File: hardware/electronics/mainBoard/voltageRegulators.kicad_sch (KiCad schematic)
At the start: 44 parts, among them J28 Conn_01x04_Pin, J29 Conn_01x04_Pin, Q10 BSS138-7-F, Q11 BSS138-7-F, Q8 CSD17581Q3A, Q9 CSD17581Q3A, U23 LM25148-Q1, U24 TPS62A01

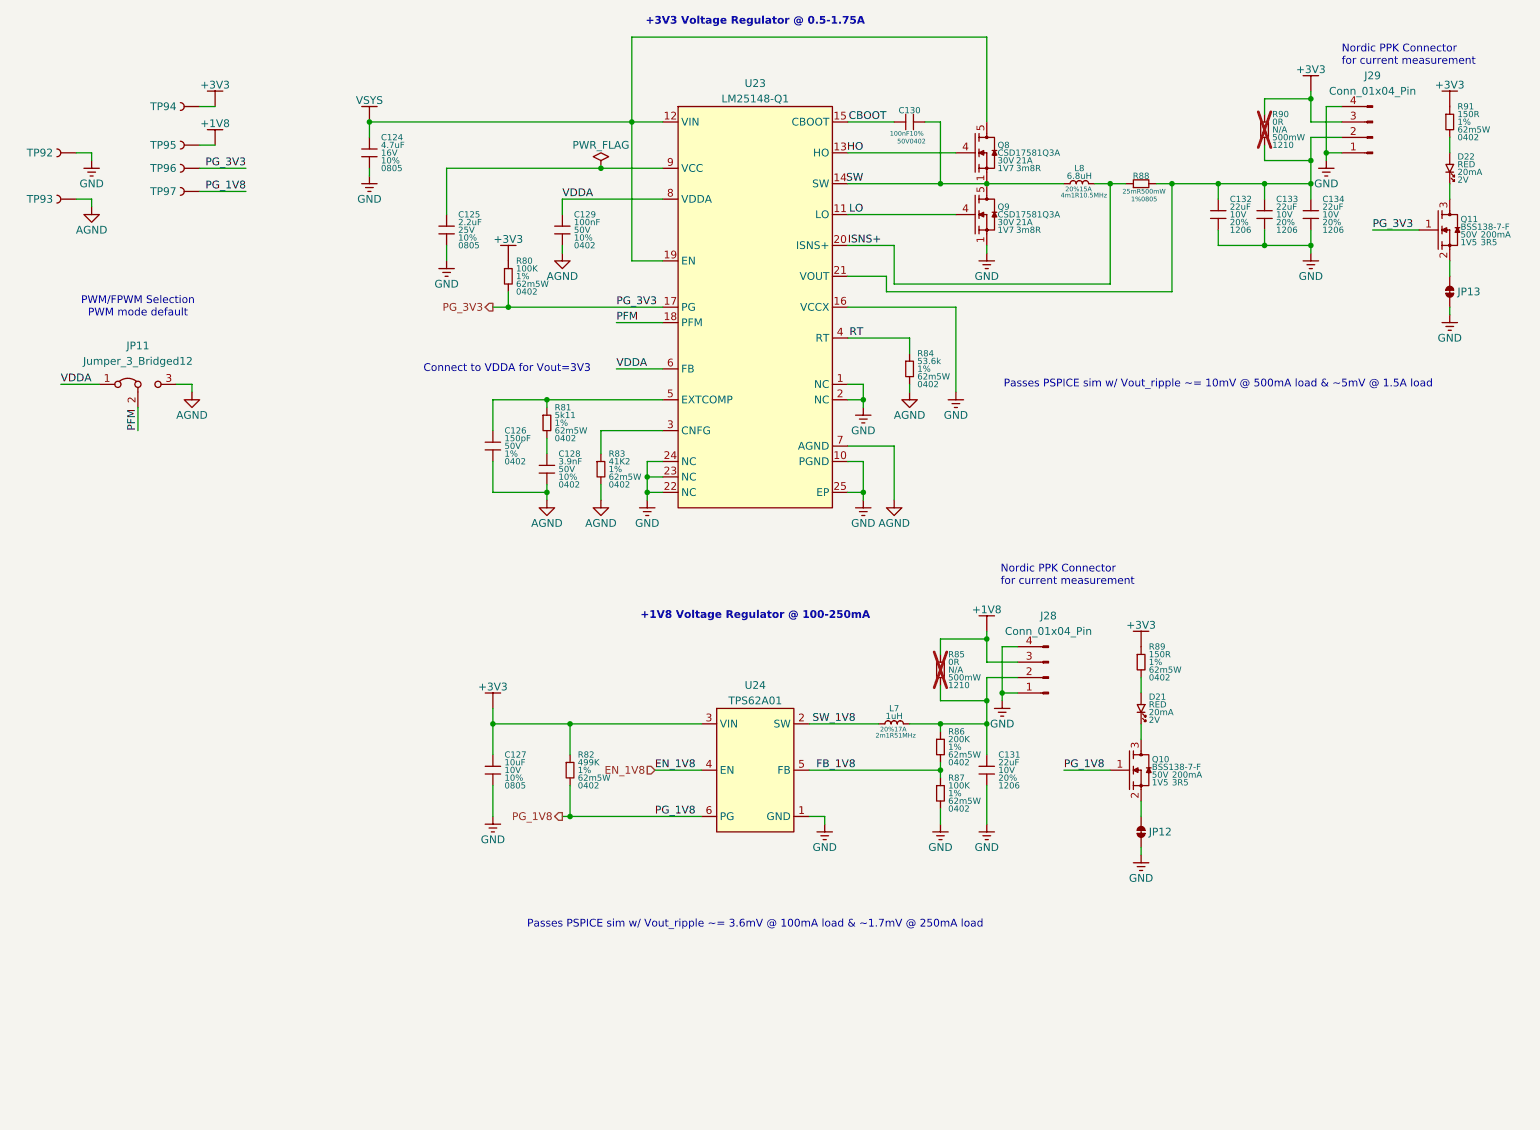
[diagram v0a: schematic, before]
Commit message: updated symbol refs
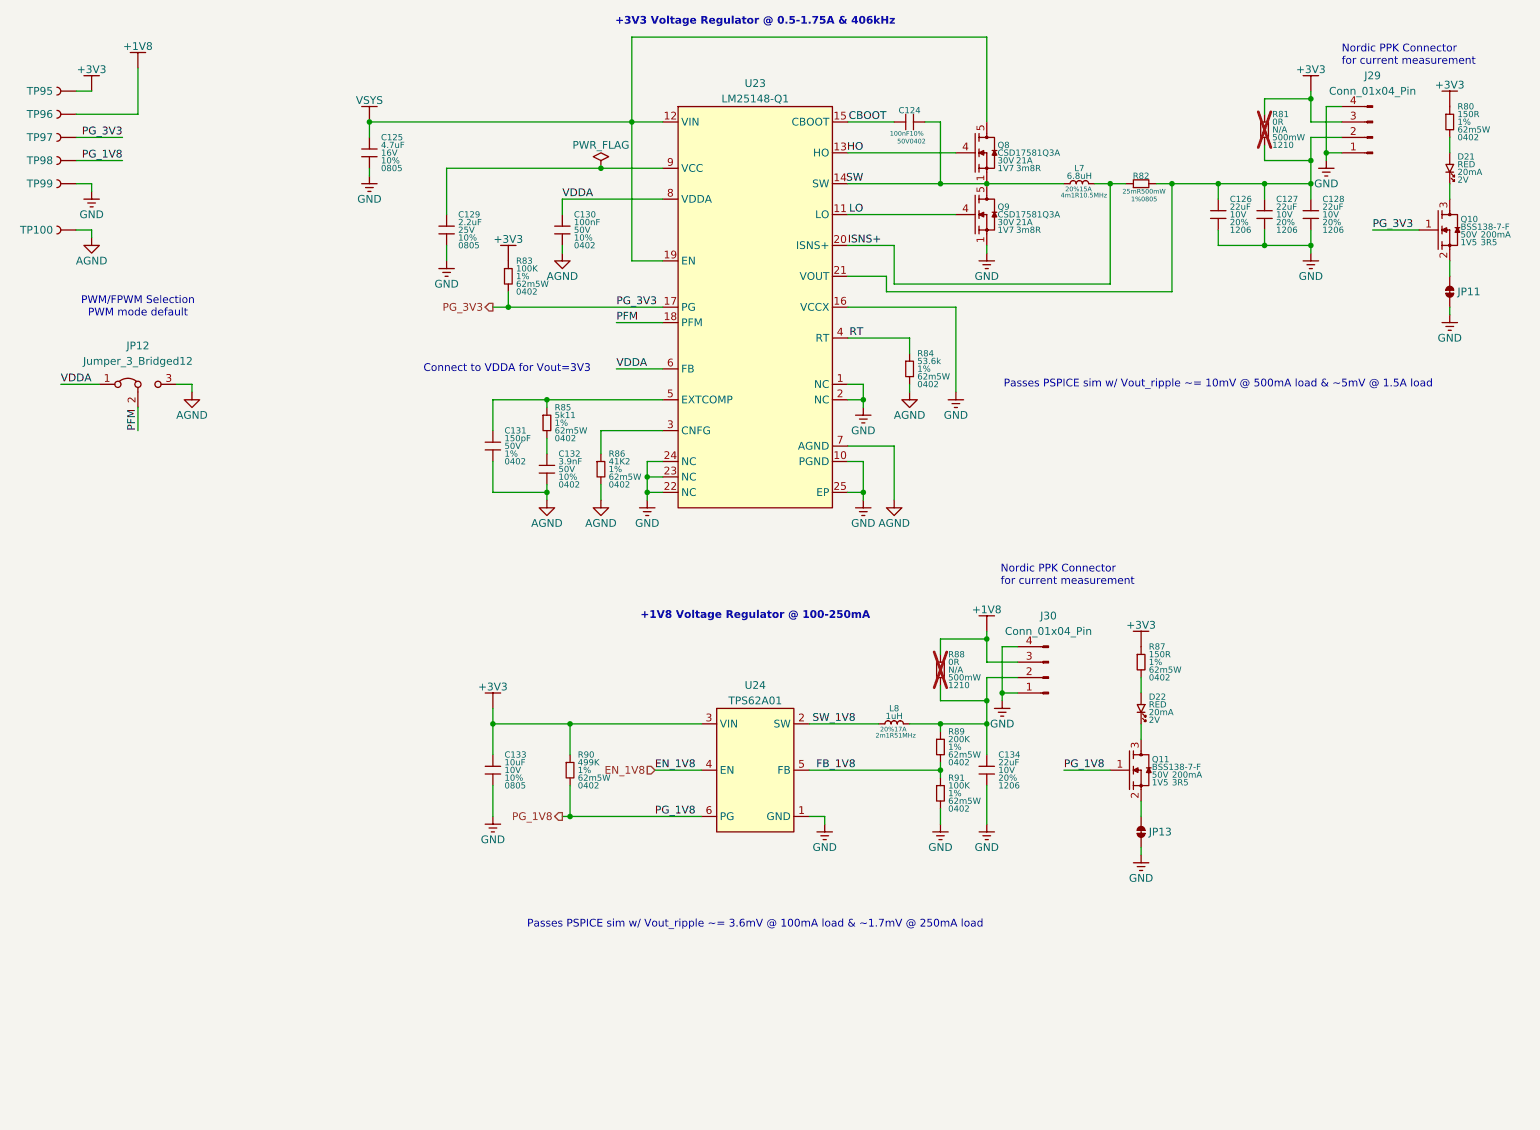
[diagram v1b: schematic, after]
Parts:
- renumbered C130 to C124, C124 to C125, C132 to C126, C133 to C127, C134 to C128, C125 to C129, C129 to C130, C126 to C131, C128 to C132, C127 to C133, C131 to C134, D22 to D21, D21 to D22, J28 to J30, JP13 to JP11, JP11 to JP12, JP12 to JP13, L8 to L7, L7 to L8, Q11 to Q10, Q10 to Q11, R91 to R80, R90 to R81, R88 to R82, R80 to R83, R81 to R85, R83 to R86, R89 to R87, R85 to R88, R86 to R89, R82 to R90, R87 to R91, TP93 to TP100, TP94 to TP95, TP95 to TP96, TP96 to TP97, TP97 to TP98, TP92 to TP99
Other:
- note added: "+3V3 Voltage Regulator @ 0.5-1.75A & 406kHz"
- note removed: "+3V3 Voltage Regulator @ 0.5-1.75A"
- moved on the sheet: TP100, TP95, TP96, TP97, TP98, TP99

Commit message: assigned FPs
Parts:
- L7: footprint (none) -> lib_passives:WE-XHMI-1510
- Q8, Q9: footprint (none) -> lib_ICs:SON65P300X315X90-8
- U23: footprint (none) -> lib_ICs:QFN50P350X550X100-24
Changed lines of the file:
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@@
 			)
 		)
-		(property "Footprint" ""
+		(property "Footprint" "lib_ICs:QFN50P350X550X100-24"
 			(at 139.7 63.5 0)
 			(effects
@@
 			)
 		)
-		(property "Footprint" ""
+		(property "Footprint" "lib_ICs:SON65P300X315X90-8"
 			(at 180.34 40.005 90)
 			(effects
@@
 			)
 		)
-		(property "Footprint" ""
+		(property "Footprint" "lib_passives:WE-XHMI-1510"
 			(at 191.77 43.18 0)
 			(effects
@@
 			)
 		)
-		(property "Footprint" ""
+		(property "Footprint" "lib_ICs:SON65P300X315X90-8"
 			(at 180.34 50.165 90)
 			(effects

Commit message: added footprints to symbols
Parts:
- J29, J30: footprint (none) -> lib_connectors:conn_01x04_254_right_angle
- JP12: footprint (none) -> lib_passives:SolderJumper-3_P1.3mm_Bridged12_RoundedPad1.0x1.5mm
- L8: footprint (none) -> lib_passives:WE-XHMI-8080
- Q10, Q11: footprint (none) -> lib_ICs:SOT23
- U24: footprint (none) -> lib_ICs:SOT563
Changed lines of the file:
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@@
 			)
 		)
-		(property "Footprint" ""
+		(property "Footprint" "lib_passives:WE-XHMI-8080"
 			(at 161.29 132.08 0)
 			(effects
@@
 			)
 		)
-		(property "Footprint" ""
+		(property "Footprint" "lib_ICs:SOT23"
 			(at 205.74 141.605 90)
 			(effects
@@
 			)
 		)
-		(property "Footprint" ""
+		(property "Footprint" "lib_connectors:conn_01x04_254_right_angle"
 			(at 241.3 35.56 0)
 			(effects
@@
 			)
 		)
-		(property "Footprint" ""
+		(property "Footprint" "lib_connectors:conn_01x04_254_right_angle"
 			(at 187.96 124.46 0)
 			(effects
@@
 			)
 		)
-		(property "Footprint" ""
+		(property "Footprint" "lib_passives:SolderJumper-3_P1.3mm_Bridged12_RoundedPad1.0x1.5mm"
 			(at 38.1 76.2 0)
 			(effects
@@
 			)
 		)
-		(property "Footprint" ""
+		(property "Footprint" "lib_ICs:SOT563"
 			(at 139.7 139.7 0)
 			(effects
@@
 			)
 		)
-		(property "Footprint" ""
+		(property "Footprint" "lib_ICs:SOT23"
 			(at 256.54 52.705 90)
 			(effects

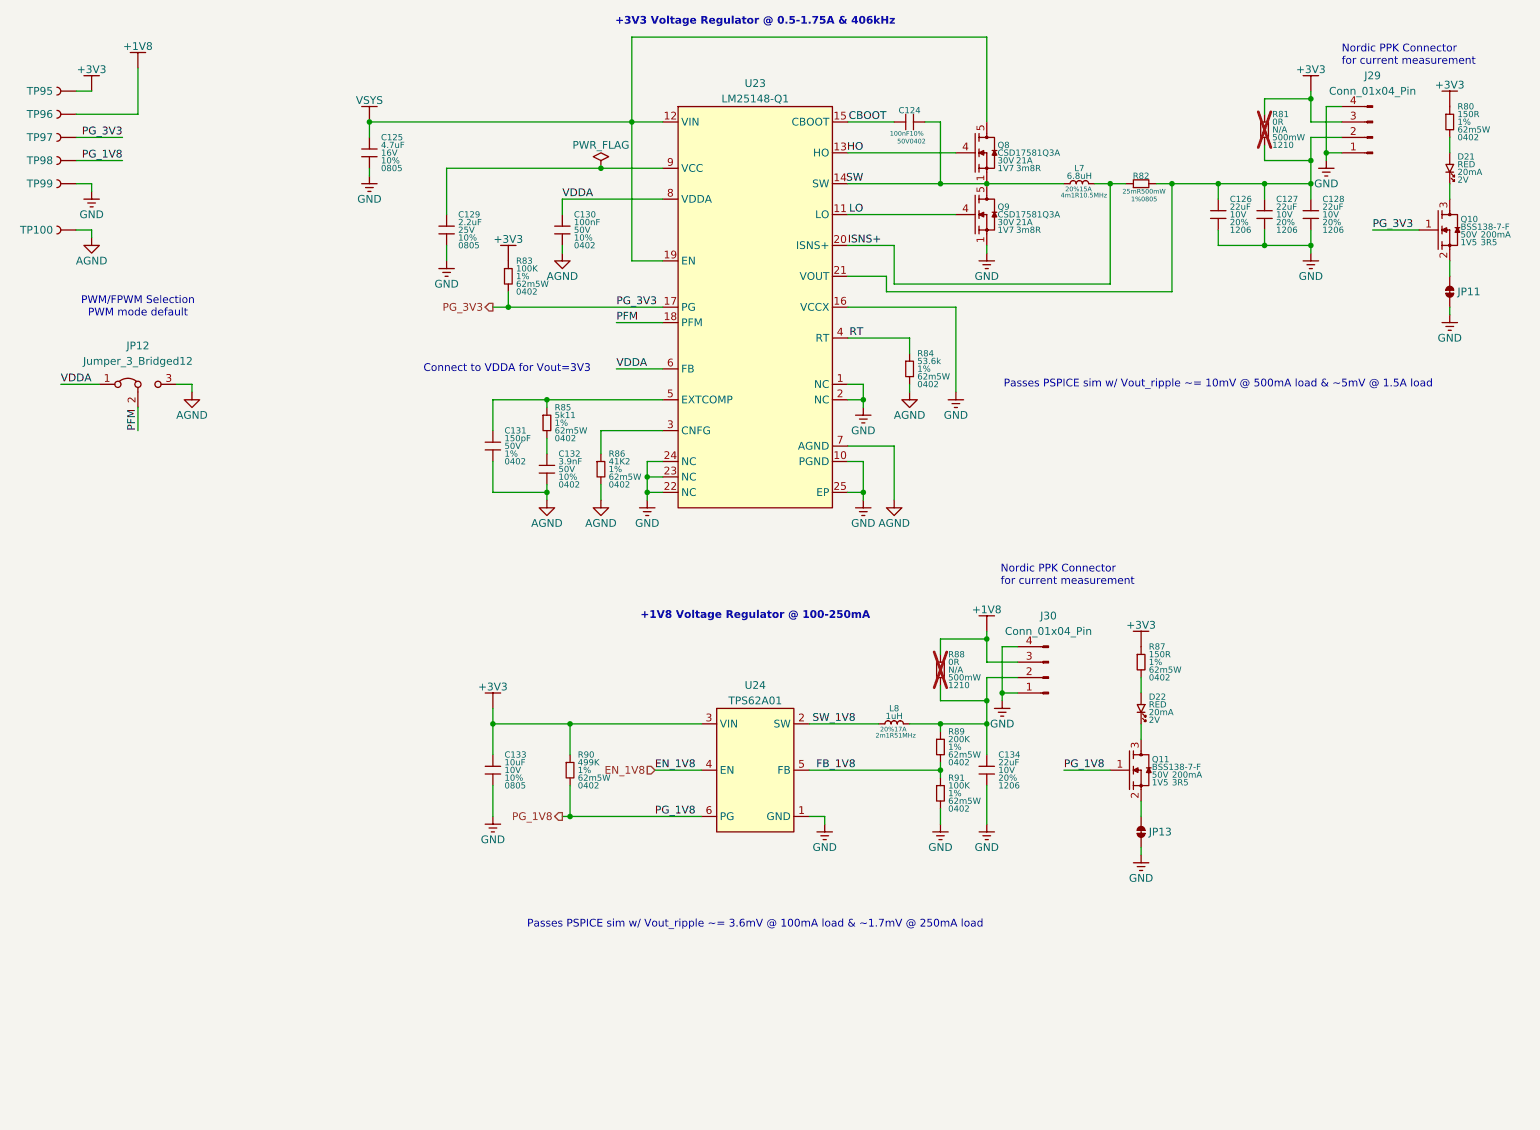
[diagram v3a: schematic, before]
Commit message: assigned footprints
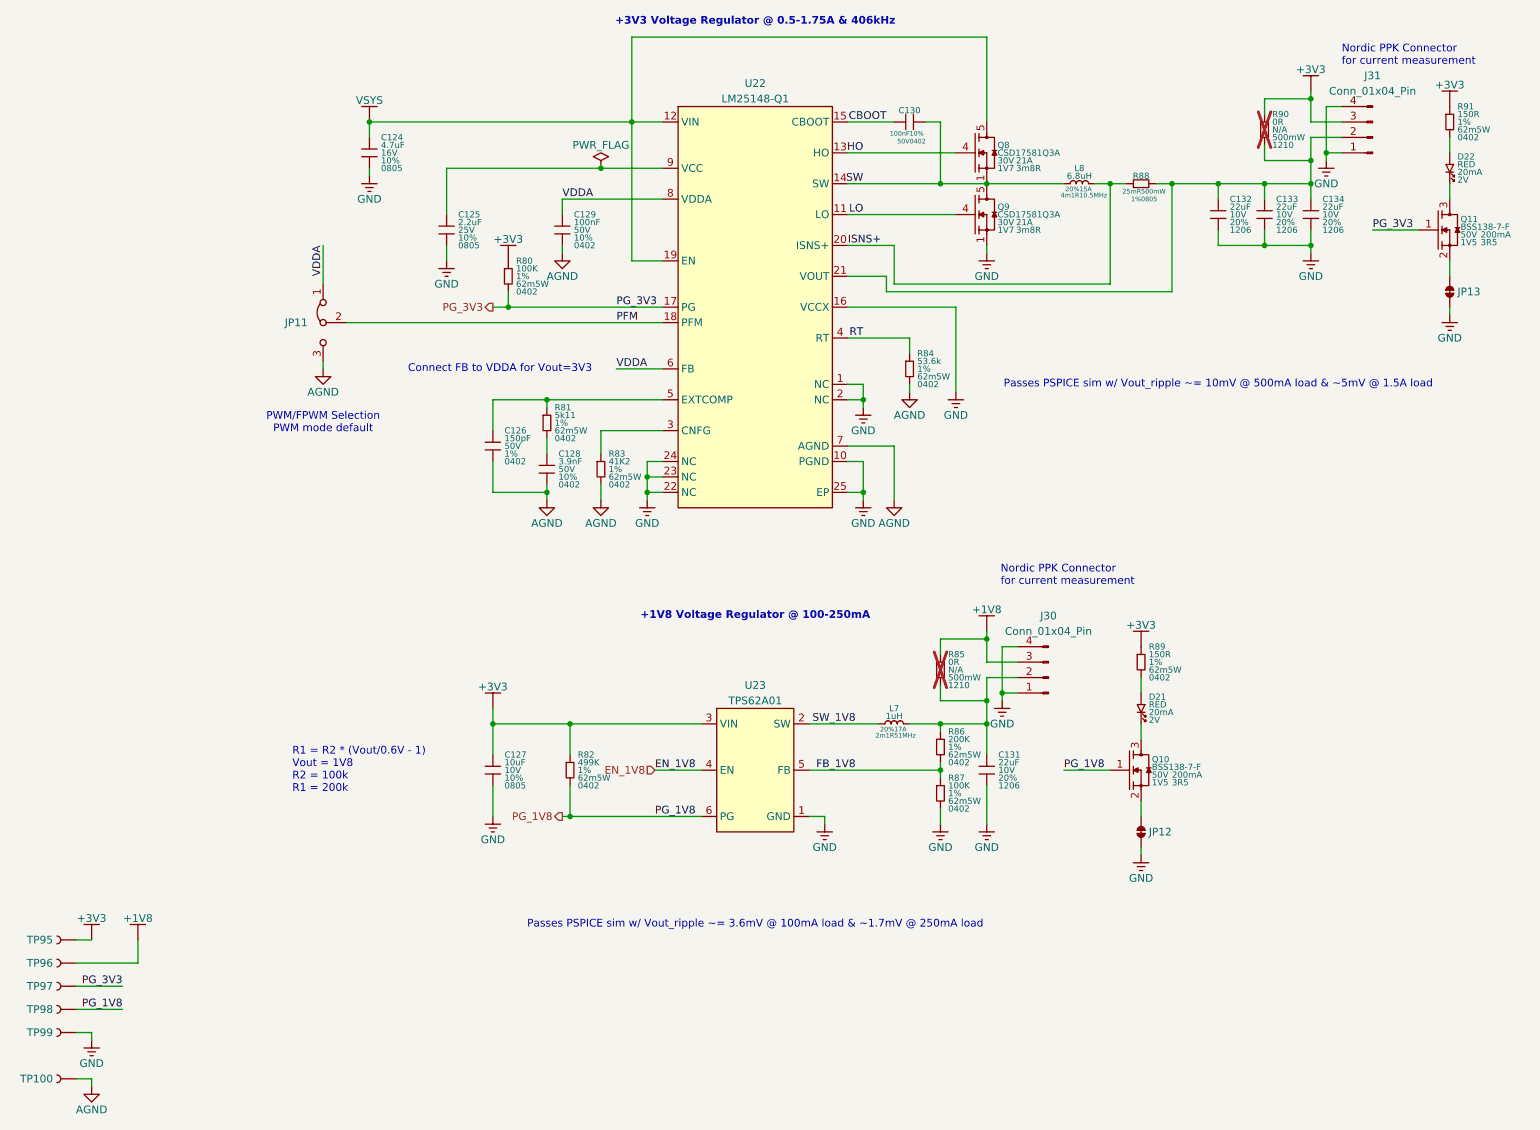
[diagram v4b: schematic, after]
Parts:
- C124: renamed from C125; footprint (none) -> lib_passives:GCM0805
- C125: renamed from C129; footprint (none) -> lib_passives:GCM0805
- C126: renamed from C131; footprint (none) -> lib_passives:GCM0402
- C127: renamed from C133; footprint (none) -> lib_passives:GCM0805
- C128: renamed from C132; footprint (none) -> lib_passives:GCM0402
- C129: renamed from C130; footprint (none) -> lib_passives:GCM0402
- C130: renamed from C124; footprint (none) -> lib_passives:GCM0402
- C131: renamed from C134; footprint (none) -> lib_passives:GCM1206
- C132: renamed from C126; footprint (none) -> lib_passives:GCM1206
- C133: renamed from C127; footprint (none) -> lib_passives:GCM1206
- C134: renamed from C128; footprint (none) -> lib_passives:GCM1206
- D21: renamed from D22; footprint (none) -> lib_diodes:LTST-0603
- D22: renamed from D21; footprint (none) -> lib_diodes:LTST-0603
- JP11: renamed from JP12; value Jumper_3_Bridged12 -> ~; footprint lib_passives:SolderJumper-3_P1.3mm_Bridged12_RoundedPad1.0x1.5mm -> lib_misc:SolderJumper-3_P1.3mm_Bridged12_RoundedPad1.0x1.5mm
- JP12: renamed from JP13; footprint (none) -> lib_misc:SolderJumper-2_P1.3mm_Bridged_RoundedPad1.0x1.5mm
- JP13: renamed from JP11; footprint (none) -> lib_misc:SolderJumper-2_P1.3mm_Bridged_RoundedPad1.0x1.5mm
- R80: renamed from R83; footprint (none) -> lib_passives:CRCW0402
- R81: renamed from R85; footprint (none) -> lib_passives:CRCW0402
- R82: renamed from R90; footprint (none) -> lib_passives:CRCW0402
- R83: renamed from R86; footprint (none) -> lib_passives:CRCW0402
- R84: footprint (none) -> lib_passives:CRCW0402
- R85: renamed from R88; footprint (none) -> lib_passives:CRCW1210
- R86: renamed from R89; footprint (none) -> lib_passives:CRCW0402
- R87: renamed from R91; footprint (none) -> lib_passives:CRCW0402
- R88: renamed from R82; footprint (none) -> lib_passives:CRCW0805
- R89: renamed from R87; footprint (none) -> lib_passives:CRCW0402
- R90: renamed from R81; footprint (none) -> lib_passives:GRT1210
- R91: renamed from R80; footprint (none) -> lib_passives:CRCW0402
- TP100, TP99: footprint (none) -> lib_misc:TP_RCW
- TP95, TP96, TP97, TP98: footprint (none) -> lib_misc:TP_2mm
- renumbered J29 to J31, L8 to L7, L7 to L8, Q11 to Q10, Q10 to Q11, U23 to U22, U24 to U23
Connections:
- net SW: now also Q9.9
- net VSYS: now also Q8.9
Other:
- note added: "Connect FB to VDDA for Vout=3V3"
- note added: "R1 = R2 * (Vout/0.6V - 1) Vout = 1V8 R2 = 100k R1 = 200k"
- note removed: "Connect to VDDA for Vout=3V3"
- moved on the sheet: JP11, TP100, TP95, TP96, TP97, TP98, TP99

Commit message: updated ref designators
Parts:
- L7: renamed from L8; footprint lib_passives:WE-XHMI-1510 -> lib_passives:WE-XHMI-1090; Current Rating 15A -> 10A5; DC Resistance 4m1R -> 7m6R; DKPN 732-10714-1-ND -> 732-10712-1-ND; MPN 74439370068 -> 74439369068; Resonant Frequency 10.5MHz -> 13MHz
- renumbered C130 to C124, C124 to C125, C132 to C126, C133 to C127, C134 to C128, C125 to C129, C129 to C130, C126 to C131, C128 to C132, C127 to C133, C131 to C134, D22 to D21, D21 to D22, J31 to J30, J30 to J31, JP13 to JP11, JP11 to JP12, JP12 to JP13, L7 to L8, Q11 to Q10, Q10 to Q11, R91 to R83, R90 to R84, R88 to R85, R80 to R86, R84 to R87, R81 to R88, R83 to R89, R89 to R90, R85 to R91, R86 to R92, R82 to R93, R87 to R94

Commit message: minor changes
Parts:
- R84: footprint lib_passives:GRT1210 -> lib_passives:CRCW1210
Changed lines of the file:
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@@
 			)
 		)
-		(property "Footprint" "lib_passives:GRT1210"
+		(property "Footprint" "lib_passives:CRCW1210"
 			(at 223.52 31.75 0)
 			(effects
